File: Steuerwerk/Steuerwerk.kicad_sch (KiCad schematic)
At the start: 331 parts, among them J1 Conn_01x04, J2 Conn_01x02, J3 Conn_01x03, J4 Conn_01x03, J5 Conn_01x02, J6 Conn_01x04, J7 Conn_01x02, J8 Conn_01x04, J9 Conn_01x02, Q1 Q_PNP_BCE, U1 74LS161, U2 74LS138, U3 74LS138, U4 74240, U5 74LS374, U6 74LS374, U7 74541, U8 74541

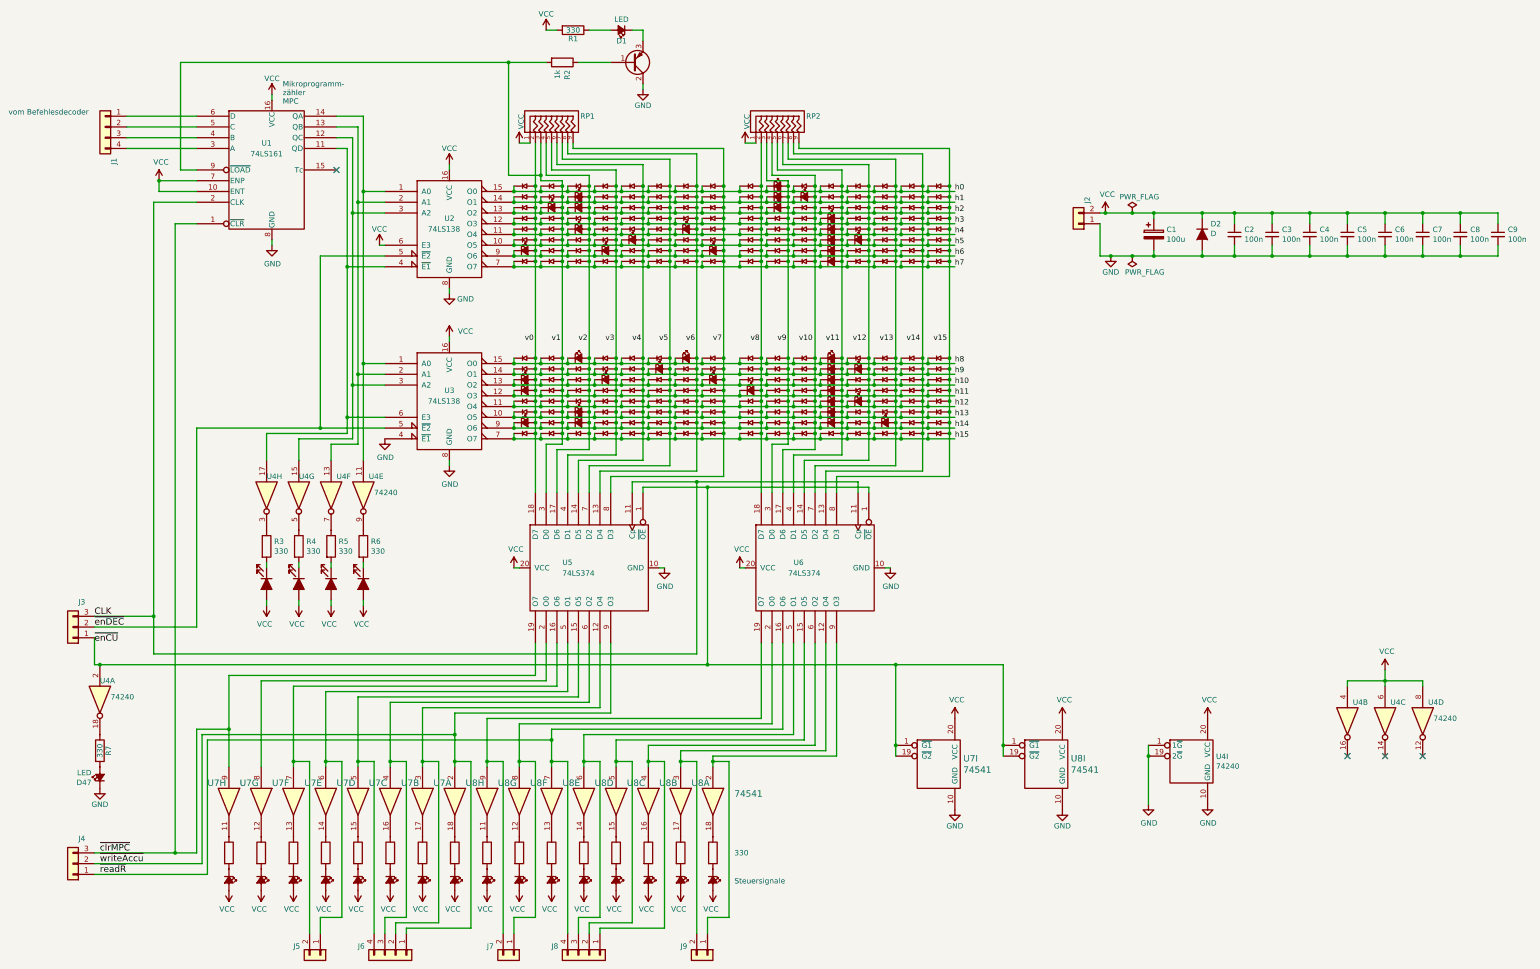
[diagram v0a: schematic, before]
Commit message: - Werte von Bauteilen in den Schaltplänen ergänzt - weitere Hinweise zum Nachbau
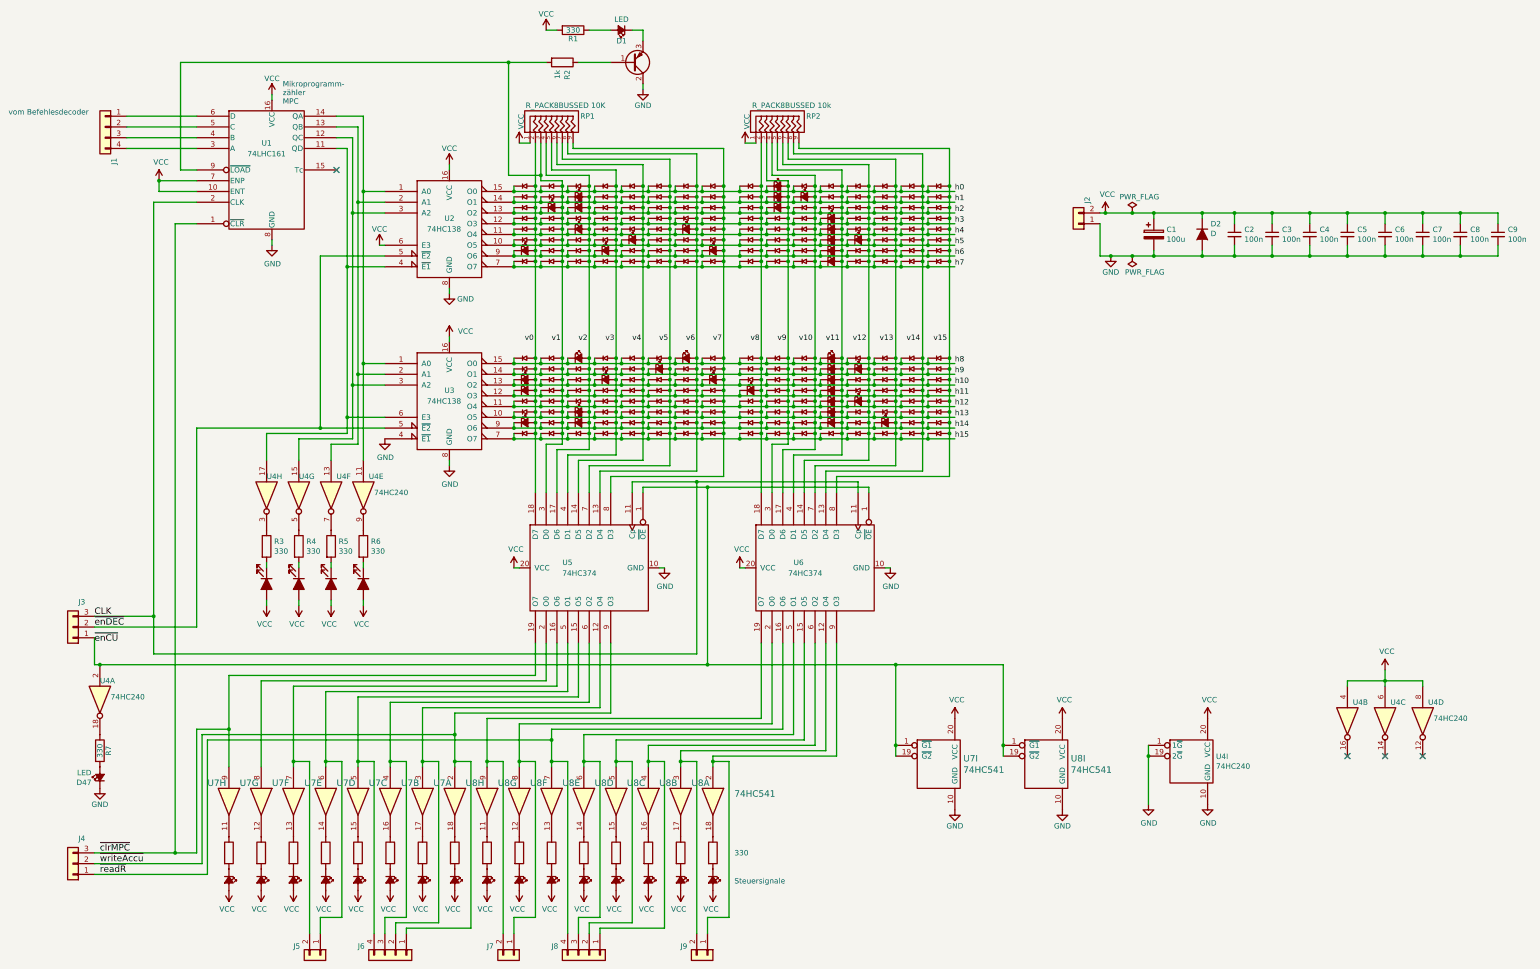
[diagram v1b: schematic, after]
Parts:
- RP1: value R_PACK8BUSSED -> R_PACK8BUSSED 10K
- RP2: value R_PACK8BUSSED -> R_PACK8BUSSED 10k
- U1: value 74LS161 -> 74LHC161
- U2, U3: value 74LS138 -> 74HC138
- U4: value 74240 -> 74HC240
- U5, U6: value 74LS374 -> 74HC374
- U7, U8: value 74541 -> 74HC541

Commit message: Alle Vorwiderstände vor LEDs in 680 Ohm geändert (Issue 5)
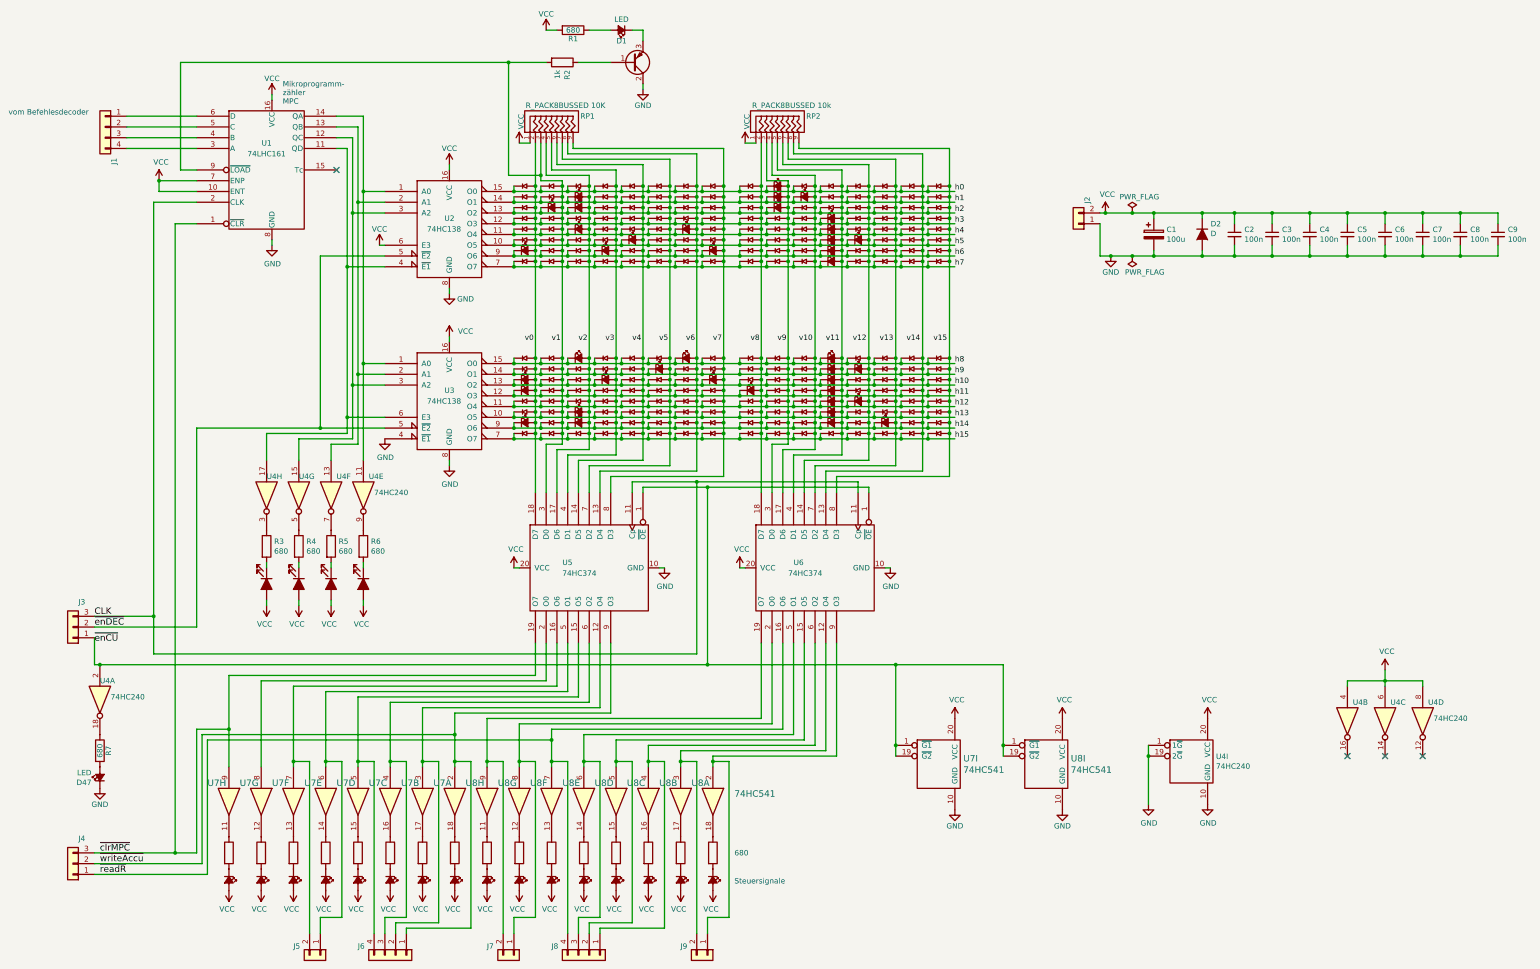
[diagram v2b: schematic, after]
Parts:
- R1, R10, R11, R12, R13, R14, R15, R16, R17, R18, R19, R20, R21, R22, R23, R3, R4, R5, R6, R7, R8, R9: value 330 -> 680
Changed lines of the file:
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@@
       (effects (font (size 1.27 1.27)) (justify left))
     )
-    (property "Value" "330" (at 100.838 148.463 0)
+    (property "Value" "680" (at 100.838 148.463 0)
       (effects (font (size 1.27 1.27)) (justify left))
     )
@@
       (effects (font (size 1.27 1.27)) (justify left))
     )
-    (property "Value" "330" (at 108.458 148.463 0)
+    (property "Value" "680" (at 108.458 148.463 0)
       (effects (font (size 1.27 1.27)) (justify left))
     )
@@
       (effects (font (size 1.27 1.27)) (justify left))
     )
-    (property "Value" "330" (at 116.078 148.463 0)
+    (property "Value" "680" (at 116.078 148.463 0)
       (effects (font (size 1.27 1.27)) (justify left))
     )
@@
       (effects (font (size 1.27 1.27)) (justify left))
     )
-    (property "Value" "330" (at 123.698 148.463 0)
+    (property "Value" "680" (at 123.698 148.463 0)
       (effects (font (size 1.27 1.27)) (justify left))
     )
@@
       (effects (font (size 1.27 1.27)) (justify left) hide)
     )
-    (property "Value" "330" (at 91.948 220.853 0)
+    (property "Value" "680" (at 91.948 220.853 0)
       (effects (font (size 1.27 1.27)) (justify left) hide)
     )
@@
       (effects (font (size 1.27 1.27)) (justify left) hide)
     )
-    (property "Value" "330" (at 99.568 220.853 0)
+    (property "Value" "680" (at 99.568 220.853 0)
       (effects (font (size 1.27 1.27)) (justify left) hide)
     )
@@
       (effects (font (size 1.27 1.27)) (justify left) hide)
     )
-    (property "Value" "330" (at 107.188 220.853 0)
+    (property "Value" "680" (at 107.188 220.853 0)
       (effects (font (size 1.27 1.27)) (justify left) hide)
     )
@@
       (effects (font (size 1.27 1.27)) (justify left) hide)
     )
-    (property "Value" "330" (at 114.808 220.853 0)
+    (property "Value" "680" (at 114.808 220.853 0)
       (effects (font (size 1.27 1.27)) (justify left) hide)
     )
@@
       (effects (font (size 1.27 1.27)) (justify left) hide)
     )
-    (property "Value" "330" (at 122.428 220.853 0)
+    (property "Value" "680" (at 122.428 220.853 0)
       (effects (font (size 1.27 1.27)) (justify left) hide)
     )
@@
       (effects (font (size 1.27 1.27)) (justify left) hide)
     )
-    (property "Value" "330" (at 130.048 220.853 0)
+    (property "Value" "680" (at 130.048 220.853 0)
       (effects (font (size 1.27 1.27)) (justify left) hide)
     )
@@
       (effects (font (size 1.27 1.27)) (justify left) hide)
     )
-    (property "Value" "330" (at 137.668 220.853 0)
+    (property "Value" "680" (at 137.668 220.853 0)
       (effects (font (size 1.27 1.27)) (justify left) hide)
     )
@@
       (effects (font (size 1.27 1.27)) (justify left) hide)
     )
-    (property "Value" "330" (at 145.288 220.853 0)
+    (property "Value" "680" (at 145.288 220.853 0)
       (effects (font (size 1.27 1.27)) (justify left) hide)
     )
@@
       (effects (font (size 1.27 1.27)) (justify left) hide)
     )
-    (property "Value" "330" (at 152.908 220.853 0)
+    (property "Value" "680" (at 152.908 220.853 0)
       (effects (font (size 1.27 1.27)) (justify left) hide)
     )
@@
       (effects (font (size 1.27 1.27)) (justify left) hide)
     )
-    (property "Value" "330" (at 160.528 220.853 0)
+    (property "Value" "680" (at 160.528 220.853 0)
       (effects (font (size 1.27 1.27)) (justify left) hide)
     )
@@
       (effects (font (size 1.27 1.27)) (justify left) hide)
     )
-    (property "Value" "330" (at 168.148 220.853 0)
+    (property "Value" "680" (at 168.148 220.853 0)
       (effects (font (size 1.27 1.27)) (justify left) hide)
     )
@@
       (effects (font (size 1.27 1.27)) (justify left) hide)
     )
-    (property "Value" "330" (at 175.768 220.853 0)
+    (property "Value" "680" (at 175.768 220.853 0)
       (effects (font (size 1.27 1.27)) (justify left) hide)
     )
@@
       (effects (font (size 1.27 1.27)) (justify left) hide)
     )
-    (property "Value" "330" (at 183.388 220.853 0)
+    (property "Value" "680" (at 183.388 220.853 0)
       (effects (font (size 1.27 1.27)) (justify left) hide)
     )
@@
       (effects (font (size 1.27 1.27)) (justify left) hide)
     )
-    (property "Value" "330" (at 191.008 220.853 0)
+    (property "Value" "680" (at 191.008 220.853 0)
       (effects (font (size 1.27 1.27)) (justify left) hide)
     )
@@
       (effects (font (size 1.27 1.27)) (justify left) hide)
     )
-    (property "Value" "330" (at 198.628 220.853 0)
+    (property "Value" "680" (at 198.628 220.853 0)
       (effects (font (size 1.27 1.27)) (justify left) hide)
     )
@@
       (effects (font (size 1.27 1.27)) (justify left) hide)
     )
-    (property "Value" "330" (at 209.55 219.71 0)
+    (property "Value" "680" (at 209.55 219.71 0)
       (effects (font (size 1.27 1.27)) (justify left))
     )
@@
       (effects (font (size 1.27 1.27)))
     )
-    (property "Value" "330" (at 171.45 25.4 90)
+    (property "Value" "680" (at 171.45 25.4 90)
       (effects (font (size 1.27 1.27)))
     )
@@
       (effects (font (size 1.27 1.27)))
     )
-    (property "Value" "330" (at 59.69 195.58 90)
-      (effects (font (size 1.27 1.27)))
-    )
+    (property "Value" "680" (at 59.69 195.58 90)
+      (effects (font (size 1.27 1.27)))
+    )
